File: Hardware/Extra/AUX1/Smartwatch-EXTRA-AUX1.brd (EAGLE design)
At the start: 18 x 25 mm, 9 parts, among them U1 UBLOX_SAM_M8Q-0-10

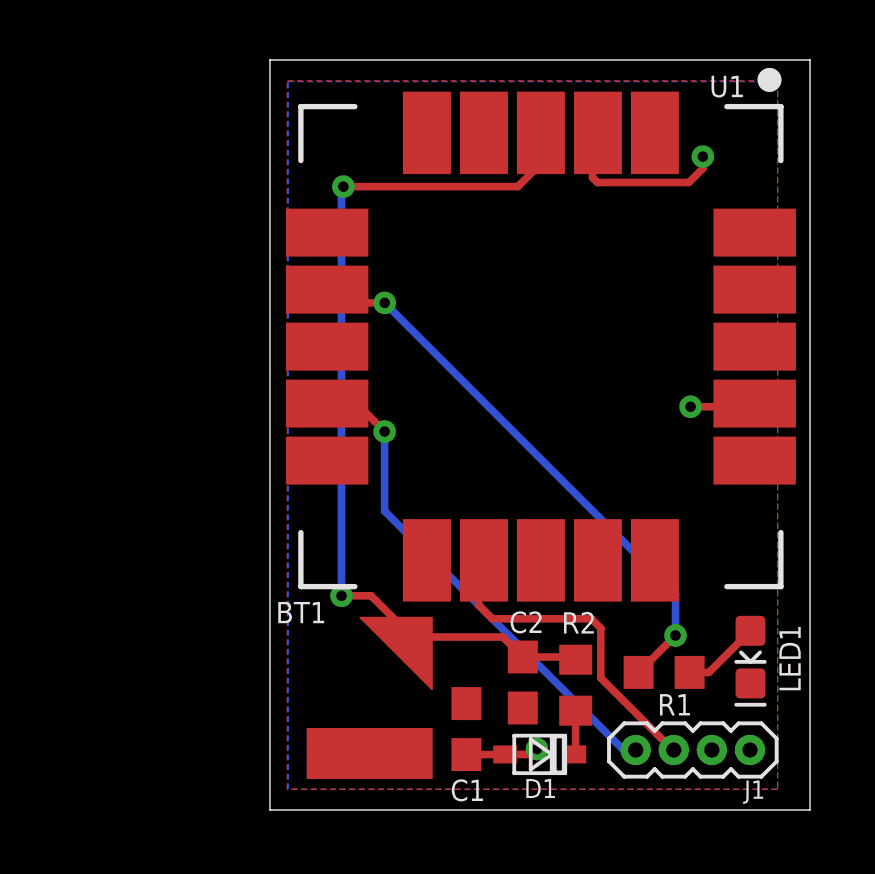
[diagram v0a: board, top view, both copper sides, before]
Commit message: Encoder changed, BOMs updated
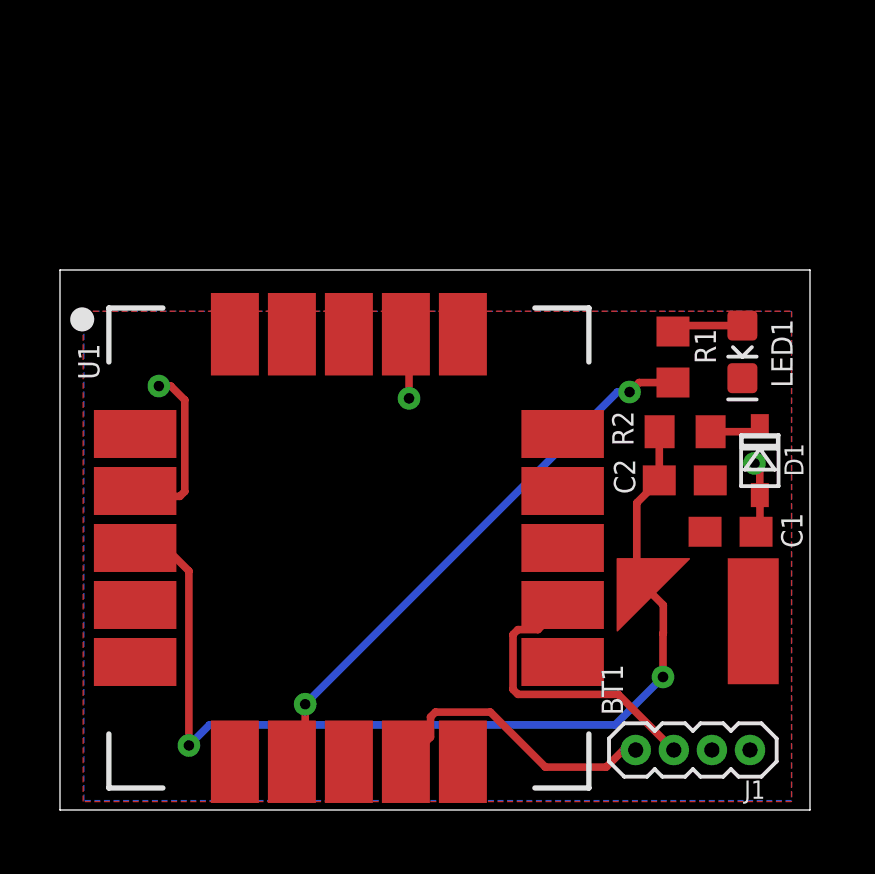
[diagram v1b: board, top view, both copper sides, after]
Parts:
- moved D1 12.2 mm to (36.3, 11.6), turned to 90 degrees
- moved BT1 11.7 mm to (34.3, 5.69), turned to 90 degrees
- moved C1 11.0 mm to (35.4, 9.27), turned to 0 degrees
- moved R1 10.5 mm to (33.4, 15.1), turned to 270 degrees
- moved LED1 10.2 mm to (35.7, 15.3)
- moved U1 9.27 mm to (22.6, 8.73), turned to 0 degrees
- moved R2 9.20 mm to (33.8, 12.6), turned to 0 degrees
- moved C2 8.63 mm to (33.8, 11.0), turned to 0 degrees
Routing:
- net SDA: track 16.6 -> 10.7 mm, vias 1 -> 0
- net BACKUP: track 30.3 -> 33.5 mm
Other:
- board size 18 x 25 mm -> 25 x 18 mm
